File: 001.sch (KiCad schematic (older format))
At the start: 36 parts, among them J1 CONN_01X02, J10 TEST_1P, J11 TEST_1P, J12 TEST_1P, J13 TEST_1P, J14 TEST_1P, J15 TEST_1P, J16 TEST_1P, J2 TEST_1P, J3 TEST_1P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

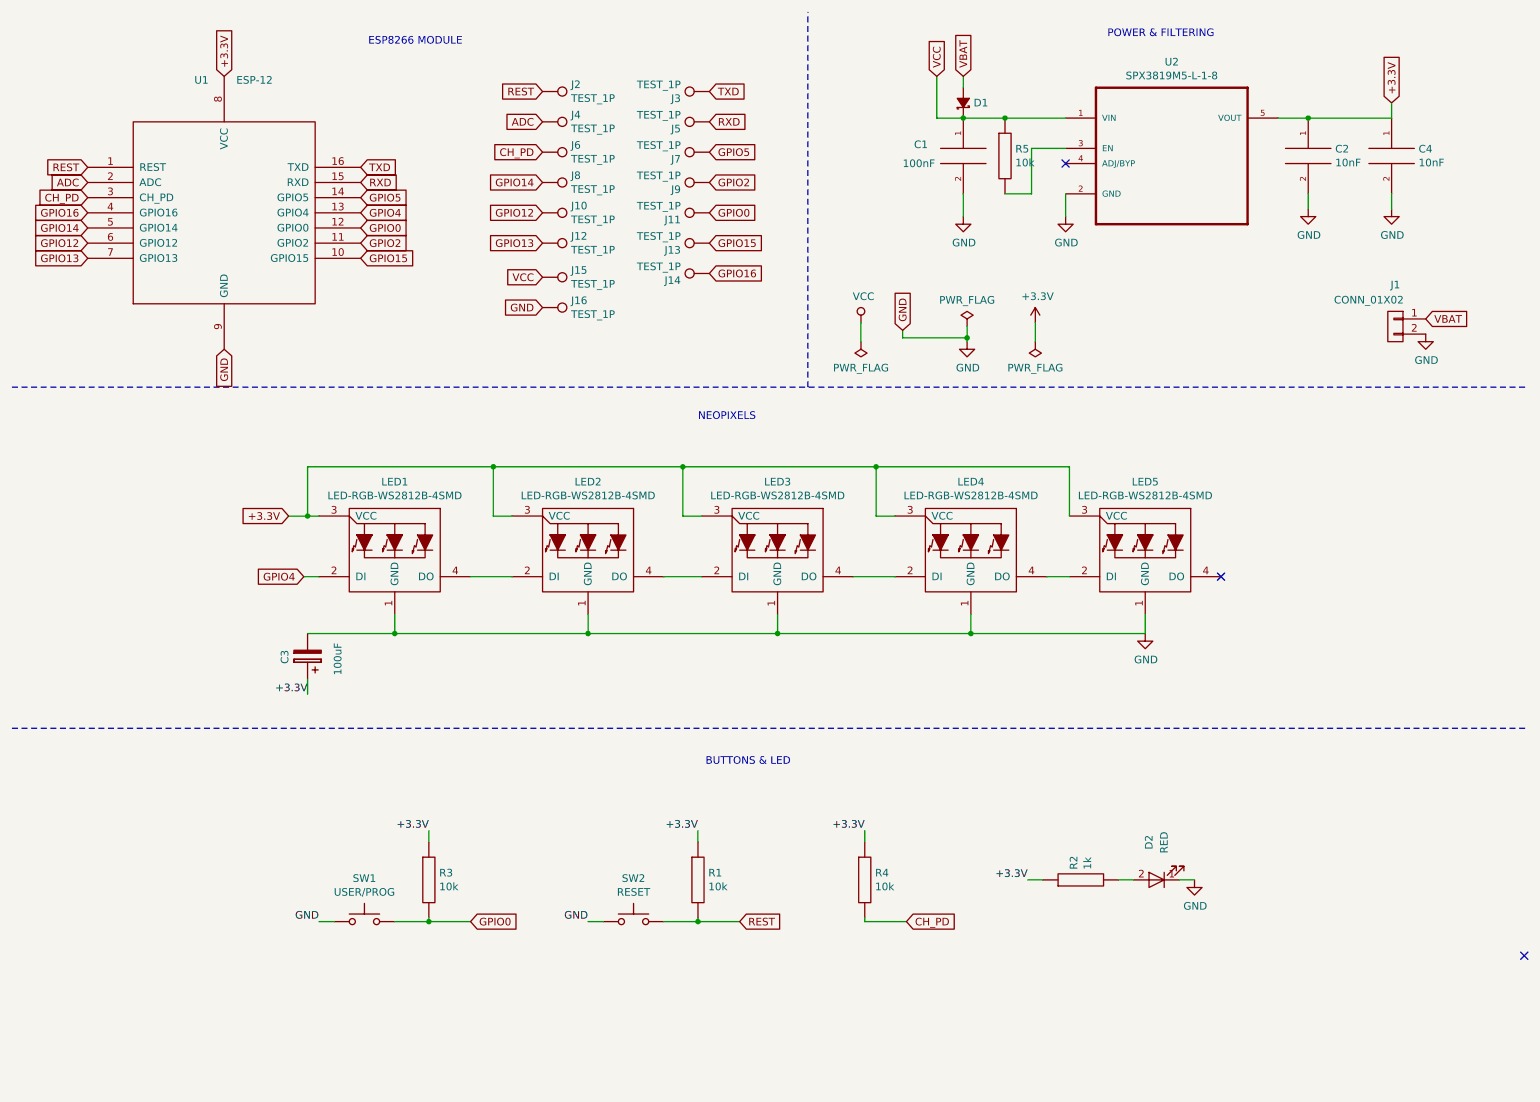
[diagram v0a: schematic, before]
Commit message: Final Release of OSHWDem Badge 2017
Final Release of OSHWDem Badge with PCBWay sponsorship
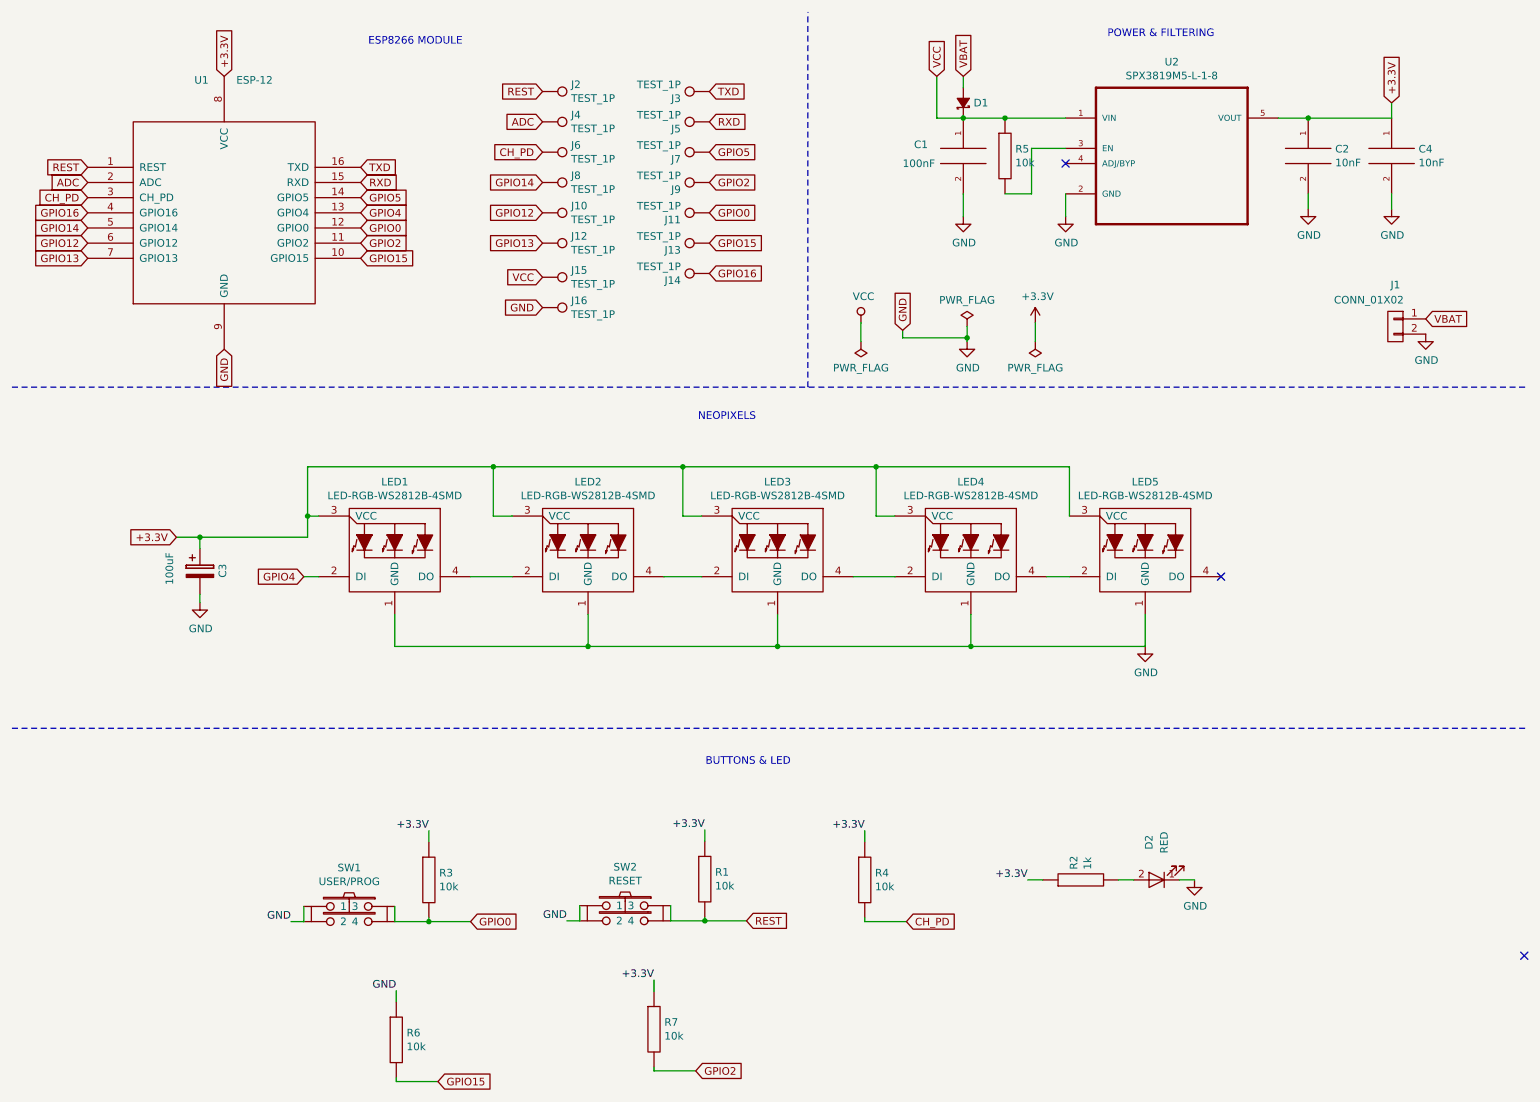
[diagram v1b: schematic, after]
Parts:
- removed SW1: USER/PROG, Wickerlib:SWITCH-OMRON-MOMENTARY-SMD-B3U-1000P, symbol SW_Push
- removed SW2: RESET, Wickerlib:SWITCH-OMRON-MOMENTARY-SMD-B3U-1000P, symbol SW_Push
- added R6, R7: 10k, Resistors_SMD:R_0805_HandSoldering, symbol R
- added SW1: USER/PROG, kmr2:SW_SPST_KMR2, symbol SWITCH-MOMENT-SPDT-SMT-B3FS-4002P
- added SW2: RESET, kmr2:SW_SPST_KMR2, symbol SWITCH-MOMENT-SPDT-SMT-B3FS-4002P
- C1, C2, C3, C4: footprint Capacitors_SMD:C_1206 -> Capacitors_SMD:C_0805_HandSoldering
- J1: footprint Connectors_Molex:Molex_PicoBlade_53261-0271_02x1.25mm_Angled -> Connectors_JST:JST_PH_S2B-PH-SM4-TB_02x2.00mm_Angled
- R1, R2, R3, R4, R5: footprint Resistors_SMD:R_1206 -> Resistors_SMD:R_0805_HandSoldering
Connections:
- net +3.3V: now also R7.1
- net GND: now also R6.1, SW1.1, SW1.2, SW2.1, SW2.2
- net GPIO0: now also SW1.3, SW1.4
- net GPIO15: now also R6.2
- net GPIO2: now also R7.2
- net REST: now also SW2.3, SW2.4
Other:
- moved on the sheet: C3
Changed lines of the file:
@@
 LIBS:ws2812b
 LIBS:SPX3819M5-L-1-8
+LIBS:kmr2
 LIBS:001-cache
 EELAYER 26 0
@@
 L CP C3
 U 1 1 595C72A9
-P 2450 4725
-F 0 "C3" V 2600 4775 50  0000 R CNN
-F 1 "100uF" V 2250 4850 50  0000 R CNN
-F 2 "Capacitors_SMD:C_1206" H 2488 4575 50  0001 C CNN
-F 3 "" H 2450 4725 50  0001 C CNN
-	1    2450 4725
-	-1   0    0    1
+P 1740 4165
+F 0 "C3" V 1890 4215 50  0000 R CNN
+F 1 "100uF" V 1540 4290 50  0000 R CNN
+F 2 "Capacitors_SMD:C_0805_HandSoldering" H 1778 4015 50  0001 C CNN
+F 3 "" H 1740 4165 50  0001 C CNN
+	1    1740 4165
+	1    0    0    -1
 $EndComp
 $Comp
 L GND #PWR03
 U 1 1 595C807D
-P 7975 4575
-F 0 "#PWR03" H 7975 4325 50  0001 C CNN
-F 1 "GND" H 7980 4402 50  0000 C CNN
-F 2 "" H 7975 4575 50  0001 C CNN
-F 3 "" H 7975 4575 50  0001 C CNN
-	1    7975 4575
-	1    0    0    -1
-$EndComp
-Text Label 2450 4975 2    50   ~ 0
-+3.3V
+P 7975 4660
+F 0 "#PWR03" H 7975 4410 50  0001 C CNN
+F 1 "GND" H 7980 4487 50  0000 C CNN
+F 2 "" H 7975 4660 50  0001 C CNN
+F 3 "" H 7975 4660 50  0001 C CNN
+	1    7975 4660
+	1    0    0    -1
+$EndComp
 Text GLabel 4000 1400 0    50   Input ~ 0
 CH_PD
@@
 Text GLabel 6600 900  1    50   Input ~ 0
 VCC
-Text GLabel 2325 3800 0    50   Input ~ 0
+Text GLabel 1585 3940 0    50   Input ~ 0
 +3.3V
 $Comp
@@
 F 0 "J1" H 9625 2825 50  0000 C CNN
 F 1 "CONN_01X02" H 9800 2725 50  0000 C CNN
-F 2 "Connectors_Molex:Molex_PicoBlade_53261-0271_02x1.25mm_Angled" H 9625 2550 50  0001 C CNN
+F 2 "Connectors_JST:JST_PH_S2B-PH-SM4-TB_02x2.00mm_Angled" H 9625 2550 50  0001 C CNN
 F 3 "" H 9625 2550 50  0001 C CNN
 	1    9625 2550
@@
 	-1   0    0    1
 $EndComp
-$Comp
-L SW_Push SW1
-U 1 1 597DE78D
-P 2825 6475
-F 0 "SW1" H 2825 6760 50  0000 C CNN
-F 1 "USER/PROG" H 2825 6669 50  0000 C CNN
-F 2 "Wickerlib:SWITCH-OMRON-MOMENTARY-SMD-B3U-1000P" H 2825 6675 50  0001 C CNN
-F 3 "" H 2825 6675 50  0001 C CNN
-	1    2825 6475
-	1    0    0    -1
-$EndComp
 Text GLabel 3525 6475 2    50   Input ~ 0
 GPIO0
@@
 F 0 "R3" H 3318 6246 50  0000 L CNN
 F 1 "10k" H 3318 6155 50  0000 L CNN
-F 2 "Resistors_SMD:R_1206" H 3250 6200 50  0001 C CNN
+F 2 "Resistors_SMD:R_0805_HandSoldering" H 3250 6200 50  0001 C CNN
 F 3 "" H 3250 6200 50  0001 C CNN
 	1    3250 6200
 	1    0    0    -1
 $EndComp
-Text Label 2525 6475 2    50   ~ 0
+Text Label 2340 6475 2    50   ~ 0
 GND
 Text Label 3250 5875 2    50   ~ 0
@@
 F 0 "C1" H 6450 1500 50  0000 L CNN
 F 1 "100nF" H 6375 1375 50  0000 L CNN
-F 2 "Capacitors_SMD:C_1206" H 6775 1425 50  0001 C CNN
+F 2 "Capacitors_SMD:C_0805_HandSoldering" H 6775 1425 50  0001 C CNN
 F 3 "" H 6775 1425 50  0001 C CNN
 	1    6775 1425
@@
 F 0 "C2" H 9228 1471 50  0000 L CNN
 F 1 "10nF" H 9228 1380 50  0000 L CNN
-F 2 "Capacitors_SMD:C_1206" H 9050 1425 50  0001 C CNN
+F 2 "Capacitors_SMD:C_0805_HandSoldering" H 9050 1425 50  0001 C CNN
 F 3 "" H 9050 1425 50  0001 C CNN
 	1    9050 1425
@@
 F 0 "R2" H 7618 6246 50  0000 L CNN
 F 1 "1k" H 7618 6155 50  0000 L CNN
-F 2 "Resistors_SMD:R_1206" H 7550 6200 50  0001 C CNN
+F 2 "Resistors_SMD:R_0805_HandSoldering" H 7550 6200 50  0001 C CNN
 F 3 "" H 7550 6200 50  0001 C CNN
 	1    7550 6200
@@
 	1    0    0    -1
 $EndComp
-$Comp
-L SW_Push SW2
-U 1 1 597ECB0D
-P 4600 6475
-F 0 "SW2" H 4600 6760 50  0000 C CNN
-F 1 "RESET" H 4600 6669 50  0000 C CNN
-F 2 "Wickerlib:SWITCH-OMRON-MOMENTARY-SMD-B3U-1000P" H 4600 6675 50  0001 C CNN
-F 3 "" H 4600 6675 50  0001 C CNN
-	1    4600 6475
-	1    0    0    -1
-$EndComp
-Text GLabel 5300 6475 2    50   Input ~ 0
-REST
-$Comp
-L R R1
-U 1 1 597ECB14
-P 5025 6200
-F 0 "R1" H 5093 6246 50  0000 L CNN
-F 1 "10k" H 5093 6155 50  0000 L CNN
-F 2 "Resistors_SMD:R_1206" H 5025 6200 50  0001 C CNN
-F 3 "" H 5025 6200 50  0001 C CNN
-	1    5025 6200
-	1    0    0    -1
-$EndComp
-Text Label 4300 6475 2    50   ~ 0
-GND
-Text Label 5025 5875 2    50   ~ 0
-+3.3V
 Text GLabel 4000 2225 0    50   Input ~ 0
 VCC
@@
 F 0 "R4" H 6193 6246 50  0000 L CNN
 F 1 "10k" H 6193 6155 50  0000 L CNN
-F 2 "Resistors_SMD:R_1206" H 6125 6200 50  0001 C CNN
+F 2 "Resistors_SMD:R_0805_HandSoldering" H 6125 6200 50  0001 C CNN
 F 3 "" H 6125 6200 50  0001 C CNN
 	1    6125 6200
@@
 F 0 "R5" H 7118 1471 50  0000 L CNN
 F 1 "10k" H 7118 1380 50  0000 L CNN
-F 2 "Resistors_SMD:R_1206" H 7050 1425 50  0001 C CNN
+F 2 "Resistors_SMD:R_0805_HandSoldering" H 7050 1425 50  0001 C CNN
 F 3 "" H 7050 1425 50  0001 C CNN
 	1    7050 1425
@@
 F 0 "C4" H 9778 1471 50  0000 L CNN
 F 1 "10nF" H 9778 1380 50  0000 L CNN
-F 2 "Capacitors_SMD:C_1206" H 9600 1425 50  0001 C CNN
+F 2 "Capacitors_SMD:C_0805_HandSoldering" H 9600 1425 50  0001 C CNN
 F 3 "" H 9600 1425 50  0001 C CNN
 	1    9600 1425
@@
 	7325 4200 7475 4200
 Wire Wire Line
-	2450 3800 2450 3475
+	2450 3940 2450 3475
 Wire Wire Line
 	6325 3800 6200 3800
@@
 Connection ~ 3675 3475
 Wire Wire Line
-	2450 4575 7975 4575
-Wire Wire Line
-	3025 4450 3025 4575
-Connection ~ 3025 4575
-Wire Wire Line
-	4300 4450 4300 4575
-Connection ~ 4300 4575
-Wire Wire Line
-	5550 4450 5550 4575
-Connection ~ 5550 4575
-Wire Wire Line
-	6825 4575 6825 4450
+	3025 4450 3025 4660
+Wire Wire Line
+	4300 4450 4300 4660
+Wire Wire Line
+	5550 4450 5550 4660
+Wire Wire Line
+	6825 4450 6825 4660
 Wire Wire Line
 	7250 2525 7250 2650
-Wire Wire Line
-	2325 3800 2525 3800
-Connection ~ 2450 3800
 Wire Wire Line
 	6100 2525 6100 2650
@@
 Connection ~ 6800 2625
 Wire Wire Line
-	2625 6475 2525 6475
-Wire Wire Line
 	3025 6475 3525 6475
 Wire Wire Line
@@
 	3250 5950 3250 5875
 Wire Wire Line
-	4400 6475 4300 6475
-Wire Wire Line
-	4800 6475 5300 6475
-Wire Wire Line
-	5025 6450 5025 6475
-Connection ~ 5025 6475
-Wire Wire Line
-	5025 5950 5025 5875
-Wire Wire Line
 	6125 6450 6125 6475
 Wire Wire Line
@@
 	7475 3475 7475 3800
 Wire Wire Line
-	2450 4875 2450 4975
-Wire Wire Line
-	7975 4575 7975 4450
-Connection ~ 6825 4575
+	7975 4450 7975 4660
 Wire Notes Line
 	5750 2950 5750 475
@@
 	0    1    1    0
 $EndComp
+Text GLabel 3310 7530 2    50   Input ~ 0
+GPIO15
+$Comp
+L R R6
+U 1 1 59827555
+P 3035 7255
+F 0 "R6" H 3103 7301 50  0000 L CNN
+F 1 "10k" H 3103 7210 50  0000 L CNN
+F 2 "Resistors_SMD:R_0805_HandSoldering" H 3035 7255 50  0001 C CNN
+F 3 "" H 3035 7255 50  0001 C CNN
+	1    3035 7255
+	1    0    0    -1
+$EndComp
+Text Label 3035 6930 2    50   ~ 0
+GND
+Wire Wire Line
+	3035 7505 3035 7530
+Wire Wire Line
+	3035 7005 3035 6930
+Wire Wire Line
+	3035 7530 3310 7530
+Text GLabel 5010 7460 2    50   Input ~ 0
+GPIO2
+$Comp
+L R R7
+U 1 1 59827AAC
+P 4735 7185
+F 0 "R7" H 4803 7231 50  0000 L CNN
+F 1 "10k" H 4803 7140 50  0000 L CNN
+F 2 "Resistors_SMD:R_0805_HandSoldering" H 4735 7185 50  0001 C CNN
+F 3 "" H 4735 7185 50  0001 C CNN
+	1    4735 7185
+	1    0    0    -1
+$EndComp
+Text Label 4735 6860 2    50   ~ 0
++3.3V
+Wire Wire Line
+	4735 7435 4735 7460
+Wire Wire Line
+	4735 6935 4735 6860
+Wire Wire Line
+	4735 7460 5010 7460
+$Comp
+L SWITCH-MOMENT-SPDT-SMT-B3FS-4002P SW1
+U 1 1 59827AA6
+P 2725 6375
+F 0 "SW1" H 2725 6630 50  0000 C CNN
+F 1 "USER/PROG" H 2725 6539 50  0000 C CNN
+F 2 "kmr2:SW_SPST_KMR2" H 2725 6025 50  0001 C CIN
+F 3 "http://www.omron.com/ecb/products/pdf/en-b3fs_4.pdf" H 2725 6375 10  0001 C CNN
+F 4 "SWITCH MOMENT SPST-NO 0.05A 24V SMT B3FS-4002P" H 2725 6025 50  0001 C CIN "Description"
+F 5 "Omron" H 2725 6025 50  0001 C CIN "MF_Name"
+F 6 "B3F-4002P" H 2725 6025 50  0001 C CIN "MF_PN"
+F 7 "Digikey" H 2725 6025 50  0001 C CIN "S1_Name"
+F 8 "SW1278CT-ND" H 2725 6025 50  0001 C CIN "S1_PN"
+	1    2725 6375
+	1    0    0    -1
+$EndComp
+Wire Wire Line
+	3025 6375 3025 6475
+Wire Wire Line
+	2425 6375 2425 6475
+Wire Wire Line
+	2425 6475 2340 6475
+Text GLabel 5345 6470 2    50   Input ~ 0
+REST
+$Comp
+L R R1
+U 1 1 59829409
+P 5070 6195
+F 0 "R1" H 5138 6241 50  0000 L CNN
+F 1 "10k" H 5138 6150 50  0000 L CNN
+F 2 "Resistors_SMD:R_0805_HandSoldering" H 5070 6195 50  0001 C CNN
+F 3 "" H 5070 6195 50  0001 C CNN
+	1    5070 6195
+	1    0    0    -1
+$EndComp
+Text Label 4160 6470 2    50   ~ 0
+GND
+Text Label 5070 5870 2    50   ~ 0
++3.3V
+Wire Wire Line
+	4845 6470 5345 6470
+Wire Wire Line
+	5070 6445 5070 6470
+Connection ~ 5070 6470
+Wire Wire Line
+	5070 5945 5070 5870
+$Comp
+L SWITCH-MOMENT-SPDT-SMT-B3FS-4002P SW2
+U 1 1 5982941A
+P 4545 6370
+F 0 "SW2" H 4545 6625 50  0000 C CNN
+F 1 "RESET" H 4545 6534 50  0000 C CNN
+F 2 "kmr2:SW_SPST_KMR2" H 4545 6020 50  0001 C CIN
+F 3 "http://www.omron.com/ecb/products/pdf/en-b3fs_4.pdf" H 4545 6370 5   0001 C CNN
+F 4 "SWITCH MOMENT SPST-NO 0.05A 24V SMT B3FS-4002P" H 4545 6020 50  0001 C CIN "Description"
+F 5 "Omron" H 4545 6020 50  0001 C CIN "MF_Name"
+F 6 "B3F-4002P" H 4545 6020 50  0001 C CIN "MF_PN"
+F 7 "Digikey" H 4545 6020 50  0001 C CIN "S1_Name"
+F 8 "SW1278CT-ND" H 4545 6020 50  0001 C CIN "S1_PN"
+	1    4545 6370
+	1    0    0    -1
+$EndComp
+Wire Wire Line
+	4845 6370 4845 6470
+Wire Wire Line
+	4245 6370 4245 6470
+Wire Wire Line
+	4245 6470 4160 6470
+Wire Wire Line
+	1585 3940 2450 3940
+Wire Wire Line
+	1740 3940 1740 4015
+Wire Wire Line
+	7975 4660 3025 4660
+Connection ~ 6825 4660
+Connection ~ 5550 4660
+Connection ~ 4300 4660
+Wire Wire Line
+	1740 4315 1740 4370
+$Comp
+L GND #PWR02
+U 1 1 59894DC3
+P 1740 4370
+F 0 "#PWR02" H 1740 4120 50  0001 C CNN
+F 1 "GND" H 1745 4197 50  0000 C CNN
+F 2 "" H 1740 4370 50  0001 C CNN
+F 3 "" H 1740 4370 50  0001 C CNN
+	1    1740 4370
+	1    0    0    -1
+$EndComp
+Wire Wire Line
+	2525 3800 2450 3800
+Connection ~ 2450 3800
+Connection ~ 1740 3940
 $EndSCHEMATC
